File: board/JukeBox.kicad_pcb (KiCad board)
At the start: 2 copper layers, 90 x 90 mm, 81 parts, among them J1 USB_C_Receptacle_USB2.0, J2 Conn_01x03, J3 Conn_01x04, J4 Conn_01x08, J5 Conn_01x01, J6 Conn_01x03, J7 Conn_01x03, J8 Conn_01x01, SW1 SW_SPST, SW10 SW_SPST, SW11 SW_SPST, SW12 SW_SPST, SW2 SW_SPST, SW3 SW_SPST, SW4 SW_SPST, SW5 SW_SPST, SW6 SW_SPST, SW7 SW_SPST, SW8 SW_SPST, SW9 SW_SPST, U1 NCP1117-3.3_SOT223, U2 W25Q128JVS, U3 RP2040, Y1 ABLS-12.000MHZ-B4-T

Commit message: minor board adjustments
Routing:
- net VBUS: track 8.61 -> 13.8 mm
- net Net-(D29-Pad2): track 0.00 -> 1.95 mm
- net Net-(D30-Pad2): track 0.00 -> 1.95 mm
- net /QSPI_SCLK: track 31.4 -> 30.9 mm
- net /QSPI_SD3: track 33.4 -> 32.9 mm
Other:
- rule pad_to_mask_clearance: 0.051 -> 0

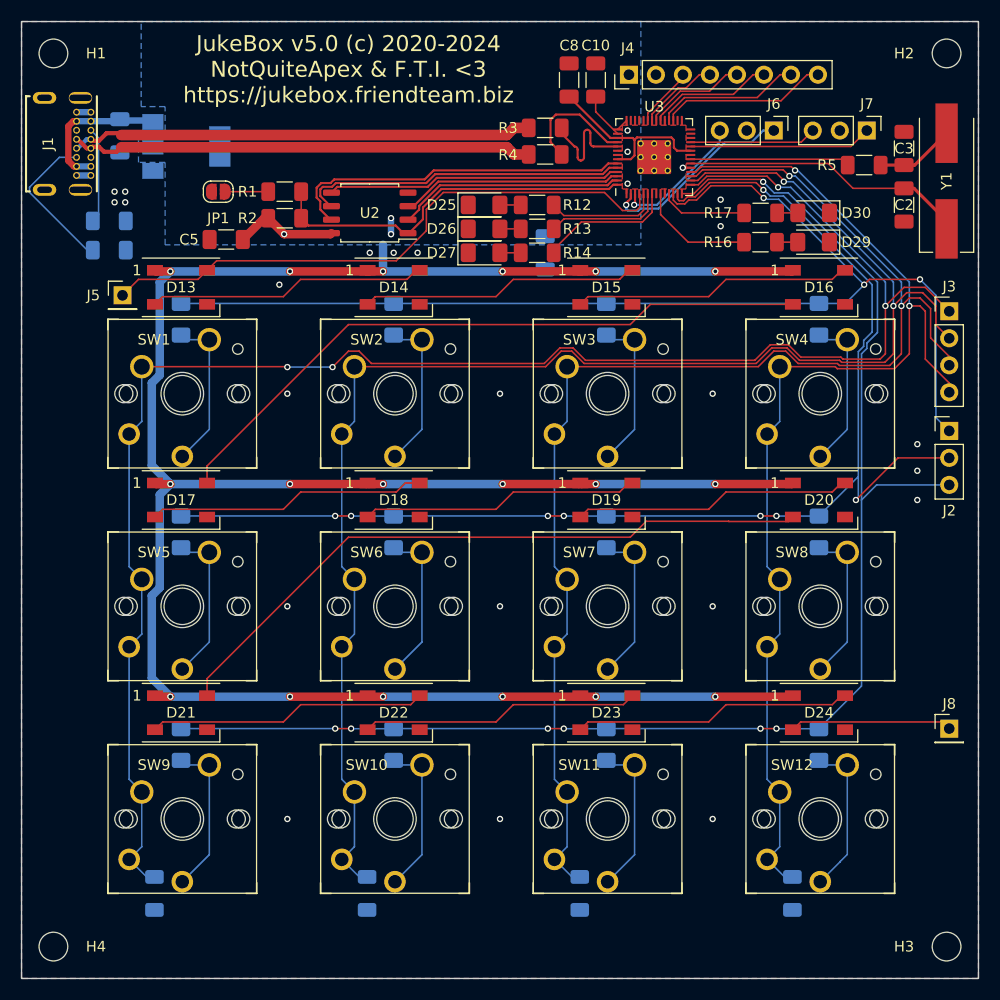
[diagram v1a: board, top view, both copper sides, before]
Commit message: move all pcb components to top layer
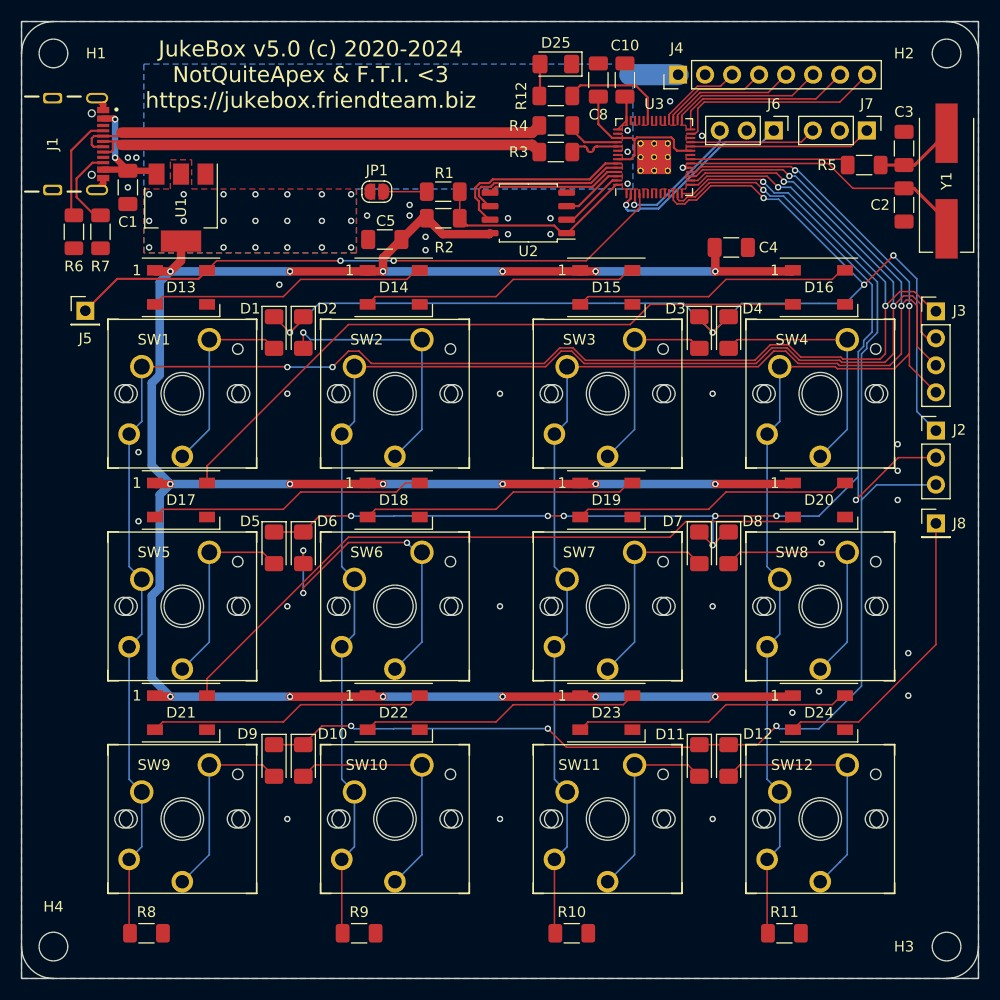
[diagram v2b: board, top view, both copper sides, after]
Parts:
- removed D26, D27, D29, D30: LED, Diode_SMD:D_1206_3216Metric_Pad1.42x1.75mm_HandSolder
- removed R13, R14, R16, R17: 200, Resistor_SMD:R_1206_3216Metric_Pad1.30x1.75mm_HandSolder
- C1, C4, D1, D10, D11, D12, D2, D3, D4, D5, D6, D7, D8, D9, R10, R11, R6, R7, R8, R9, U1: moved to F.Cu
- J1: value USB_C_Receptacle_USB2.0 -> USB4105-GF-A; footprint RP2040_minimal:GCT_USB4085-GF-A_REVA4 -> RP2040_minimal:GCT_USB4105-GF-A
- moved J8 19.3 mm to (253.6, 102.2)
- moved C4 17.5 mm to (234.3, 76.2), turned to 0 degrees
- moved C5 14.9 mm to (201.8, 75.5)
- moved JP1 14.9 mm to (201.0, 71.0)
- moved R1 14.9 mm to (207.3, 71.0)
- moved R2 14.9 mm to (207.3, 73.5)
- moved U2 14.9 mm to (215.3, 73.0)
- moved D25 14.9 mm to (217.8, 59.0), turned to 180 degrees
- moved R12 10.4 mm to (217.8, 62.0)
- moved D11 8.88 mm to (231.3, 124.5)
- moved D5 8.88 mm to (191.3, 104.5)
- moved D7 8.88 mm to (231.3, 104.5)
- moved D9 8.88 mm to (191.3, 124.5)
- moved D1 8.84 mm to (191.3, 84.2)
- moved D3 8.84 mm to (231.3, 84.2)
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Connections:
- J4 pad 3: /GPIO25 -> /GPIO21
- J4 pad 4: /GPIO24 -> /GPIO20
- J4 pad 5: /GPIO23 -> /GPIO19
- J4 pad 6: /GPIO22 -> /GPIO18
- J4 pad 7: /GPIO21 -> /GPIO17
- J4 pad 8: /GPIO20 -> /GPIO16
- R12 pad 1: /GPIO3 -> /GPIO25
- U3 pad 26: /RUN -> +3V3
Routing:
- net /GPIO16: track 0.00 -> 20.1 mm
- net /GPIO17: track 0.00 -> 17.2 mm
- net Net-(D6-Pad2): track 14.9 -> 31.1 mm, vias 0 -> 3
- net /QSPI_SS: track 35.4 -> 19.8 mm
- net /QSPI_SD1: track 21.4 -> 6.32 mm
- net /QSPI_SD0: track 27.7 -> 12.8 mm
- net /QSPI_SD3: track 32.9 -> 18.0 mm
- net /QSPI_SD2: track 20.9 -> 5.96 mm
- net /QSPI_SCLK: track 30.9 -> 16.0 mm
- net /GPIO18: track 0.00 -> 14.4 mm
- net /RGBDOUT: track 15.3 -> 28.2 mm
- net /GPIO5: track 12.8 -> 0.00 mm
- net /GPIO19: track 0.00 -> 12.3 mm
- net /GPIO22: track 11.8 -> 0.00 mm
- net /GPIO4: track 11.2 -> 0.00 mm
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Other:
- outline, holes or cut-outs redrawn

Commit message: add models to pcb, adjust some resistor placement
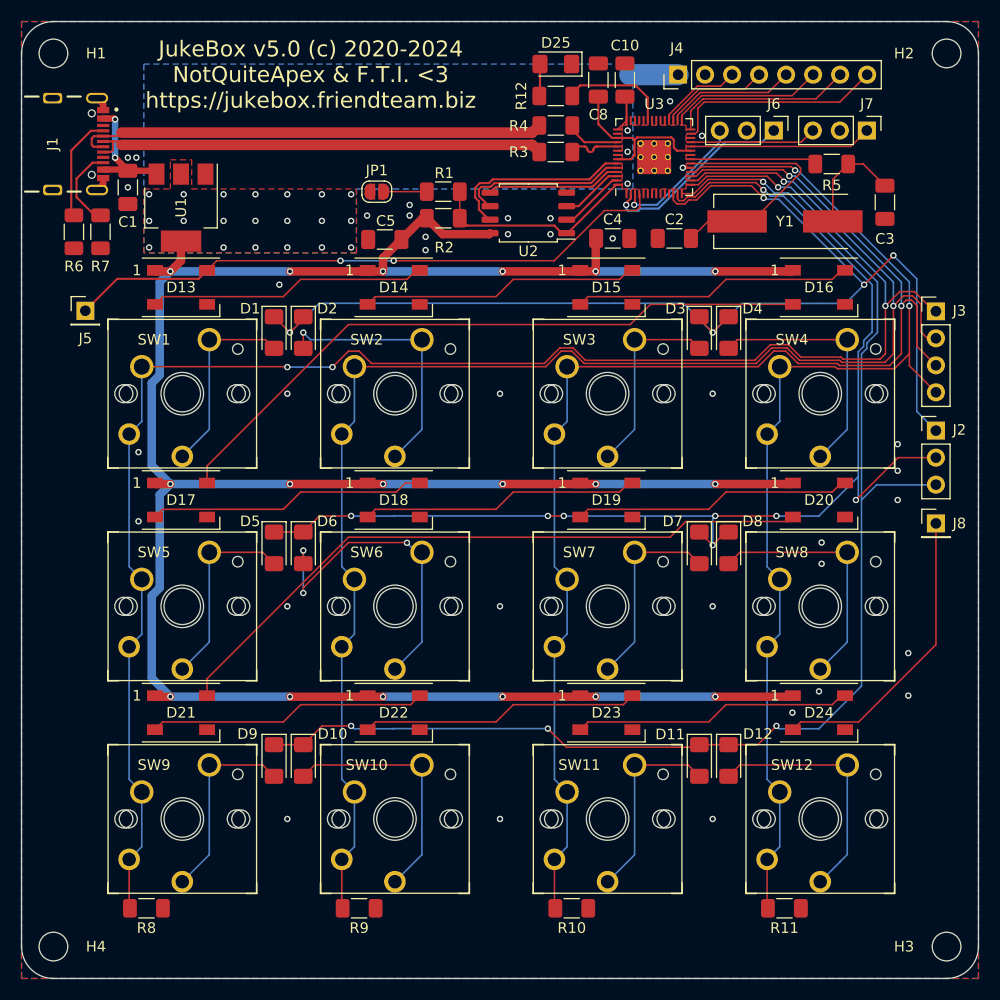
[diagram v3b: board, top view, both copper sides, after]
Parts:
- moved C2 21.8 mm to (229.0, 75.4), turned to 180 degrees
- moved Y1 15.7 mm to (239.4, 73.8), turned to 0 degrees
- moved C4 11.2 mm to (223.2, 75.4)
- moved C3 5.37 mm to (248.8, 72.0), turned to -90 degrees
- moved R5 3.05 mm to (243.8, 68.4)
- moved R10 2.35 mm to (219.3, 138.4)
- moved R11 2.35 mm to (239.3, 138.4)
- moved R8 2.35 mm to (179.3, 138.4)
- moved R9 2.35 mm to (199.3, 138.4)
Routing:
- net /XOUT: track 15.0 -> 11.9 mm
- net Net-(C3-Pad1): track 7.44 -> 10.3 mm
- net /XIN: track 27.0 -> 24.6 mm
- net /GPIO13: track 147.0 -> 144.7 mm
- net /GPIO14: track 128.3 -> 126.0 mm
- net /GPIO15: track 105.3 -> 103.0 mm
- net /GPIO12: track 164.9 -> 162.5 mm
- net +3V3: track 255.1 -> 256.0 mm
- net GND: vias 36 -> 37
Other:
- outline, holes or cut-outs redrawn

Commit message: minor adjustments
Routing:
- net /XIN: track 24.6 -> 23.8 mm
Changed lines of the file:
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@@
       (viasonmask false)
       (mode 1)
-      (useauxorigin false)
+      (useauxorigin true)
       (hpglpennumber 1)
       (hpglpenspeed 20)
@@
     (fp_line (start -1.6 -0.4) (end -1.6 0.8) (layer "F.Fab") (width 0.1))
     (fp_line (start 1.6 0.8) (end 1.6 -0.8) (layer "F.Fab") (width 0.1))
-    (pad "1" smd roundrect (at -1.4875 0 180) (size 1.425 1.75) (layers "F.Cu" "F.Paste" "F.Mask") (roundrect_rratio 0.175439)
+    (pad "1" smd roundrect (at -1.4875 0 180) (size 1.425 1.75) (layers "F.Cu" "F.Paste" "F.Mask") (roundrect_rratio 0.1754392982)
       (net 1 "GND") (pinfunction "K") (pintype "passive"))
-    (pad "2" smd roundrect (at 1.4875 0 180) (size 1.425 1.75) (layers "F.Cu" "F.Paste" "F.Mask") (roundrect_rratio 0.175439)
+    (pad "2" smd roundrect (at 1.4875 0 180) (size 1.425 1.75) (layers "F.Cu" "F.Paste" "F.Mask") (roundrect_rratio 0.1754392982)
       (net 69 "Net-(D25-Pad2)") (pinfunction "A") (pintype "passive"))
     (model "${KICAD6_3DMODEL_DIR}/Diode_SMD.3dshapes/D_1206_3216Metric.wrl"
@@
     (fp_line (start 1.6 -0.8) (end 1.6 0.8) (layer "F.Fab") (width 0.1))
     (fp_line (start -1.6 -0.8) (end 1.6 -0.8) (layer "F.Fab") (width 0.1))
-    (pad "1" smd roundrect (at -1.55 0 180) (size 1.3 1.75) (layers "F.Cu" "F.Paste" "F.Mask") (roundrect_rratio 0.192308)
+    (pad "1" smd roundrect (at -1.55 0 180) (size 1.3 1.75) (layers "F.Cu" "F.Paste" "F.Mask") (roundrect_rratio 0.1923076923)
       (net 73 "/GPIO25") (pintype "passive"))
-    (pad "2" smd roundrect (at 1.55 0 180) (size 1.3 1.75) (layers "F.Cu" "F.Paste" "F.Mask") (roundrect_rratio 0.192308)
+    (pad "2" smd roundrect (at 1.55 0 180) (size 1.3 1.75) (layers "F.Cu" "F.Paste" "F.Mask") (roundrect_rratio 0.1923076923)
       (net 69 "Net-(D25-Pad2)") (pintype "passive"))
     (model "${KICAD6_3DMODEL_DIR}/Resistor_SMD.3dshapes/R_1206_3216Metric.wrl"
@@
   (via (at 176.39 67.8) (size 0.6) (drill 0.35) (layers "F.Cu" "B.Cu") (net 2))
   (segment (start 176.39 64.2) (end 176.39 67.8) (width 0.6) (layer "B.Cu") (net 2))
-  (segment (start 235.682463 74.4) (end 234.89 74.4) (width 0.15) (layer "F.Cu") (net 3))
   (segment (start 230.5275 68.35) (end 240.432463 68.35) (width 0.15) (layer "F.Cu") (net 3))
   (segment (start 232.1525 73.8) (end 230.5525 75.4) (width 0.15) (layer "F.Cu") (net 3))
@@
     (polygon
       (pts
-        (xy 183.59 70.75)
+        (xy 183.39 70.75)
         (xy 199.09 70.75)
         (xy 199.09 76.75)
         (xy 179.09 76.75)
         (xy 179.09 70.75)
-        (xy 181.59 70.75)
-        (xy 181.59 69.75)
-        (xy 181.59 68.75)
-        (xy 181.59 68)
-        (xy 183.59 68)
+        (xy 181.79 70.75)
+        (xy 181.79 69.75)
+        (xy 181.79 68.75)
+        (xy 181.79 68.4)
+        (xy 183.39 68.4)
       )
     )

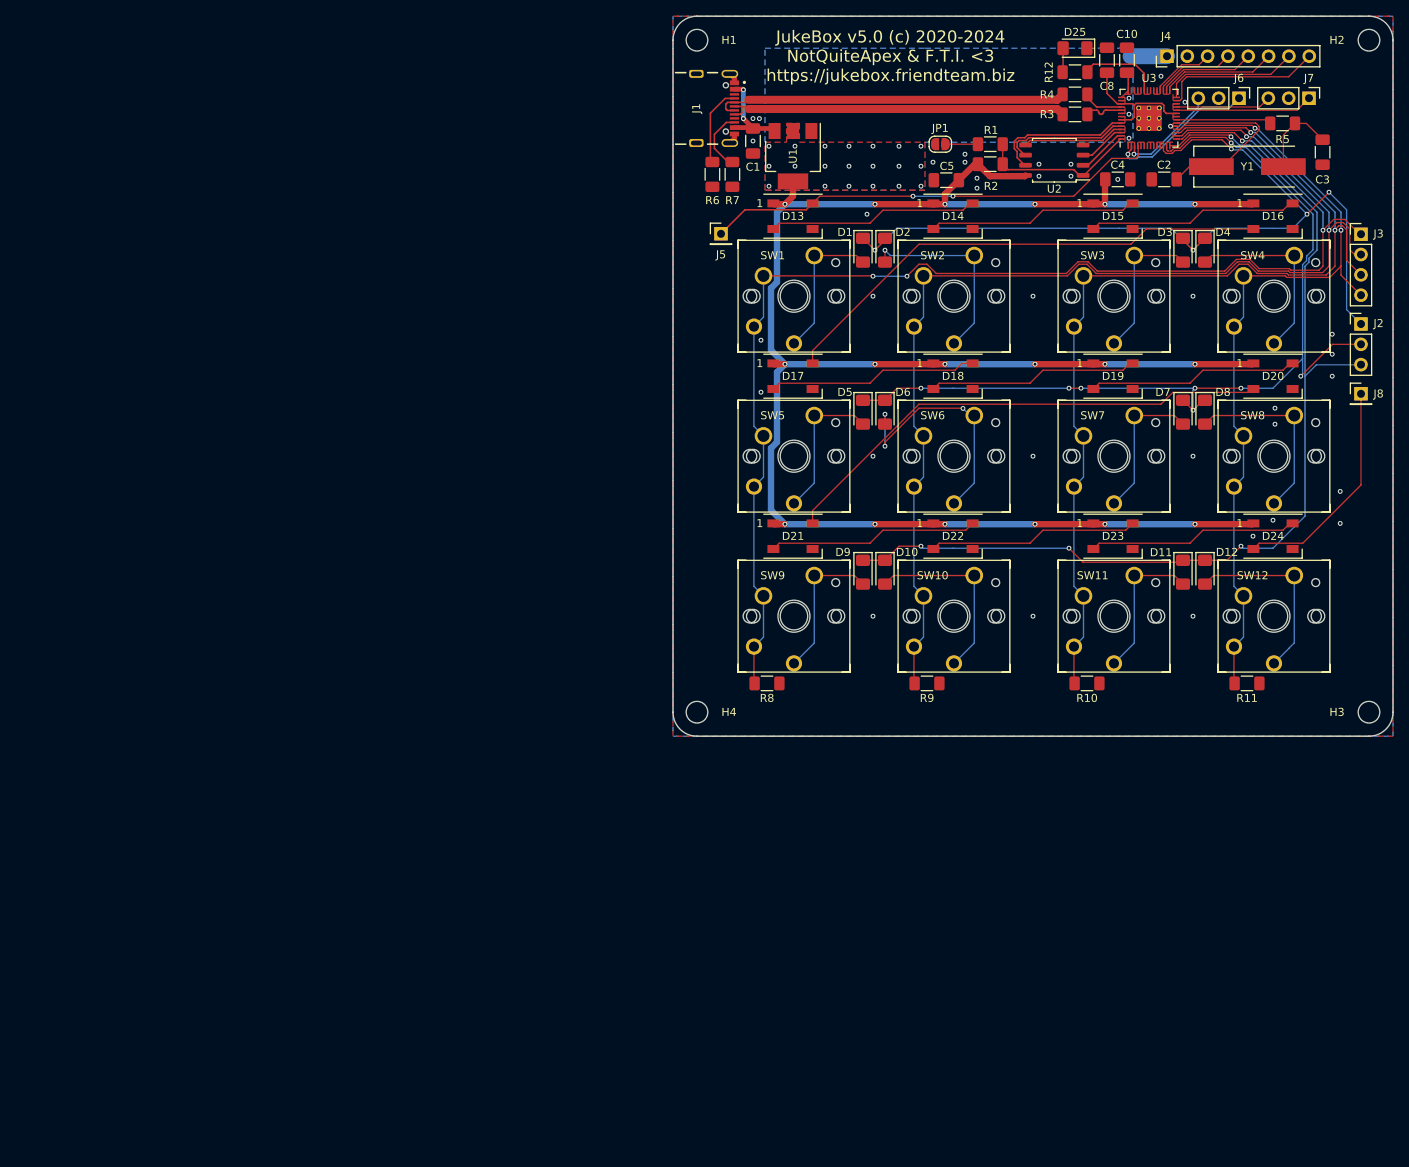
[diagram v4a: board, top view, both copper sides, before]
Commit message: fix pcb for new footprints, remove old files, update readme
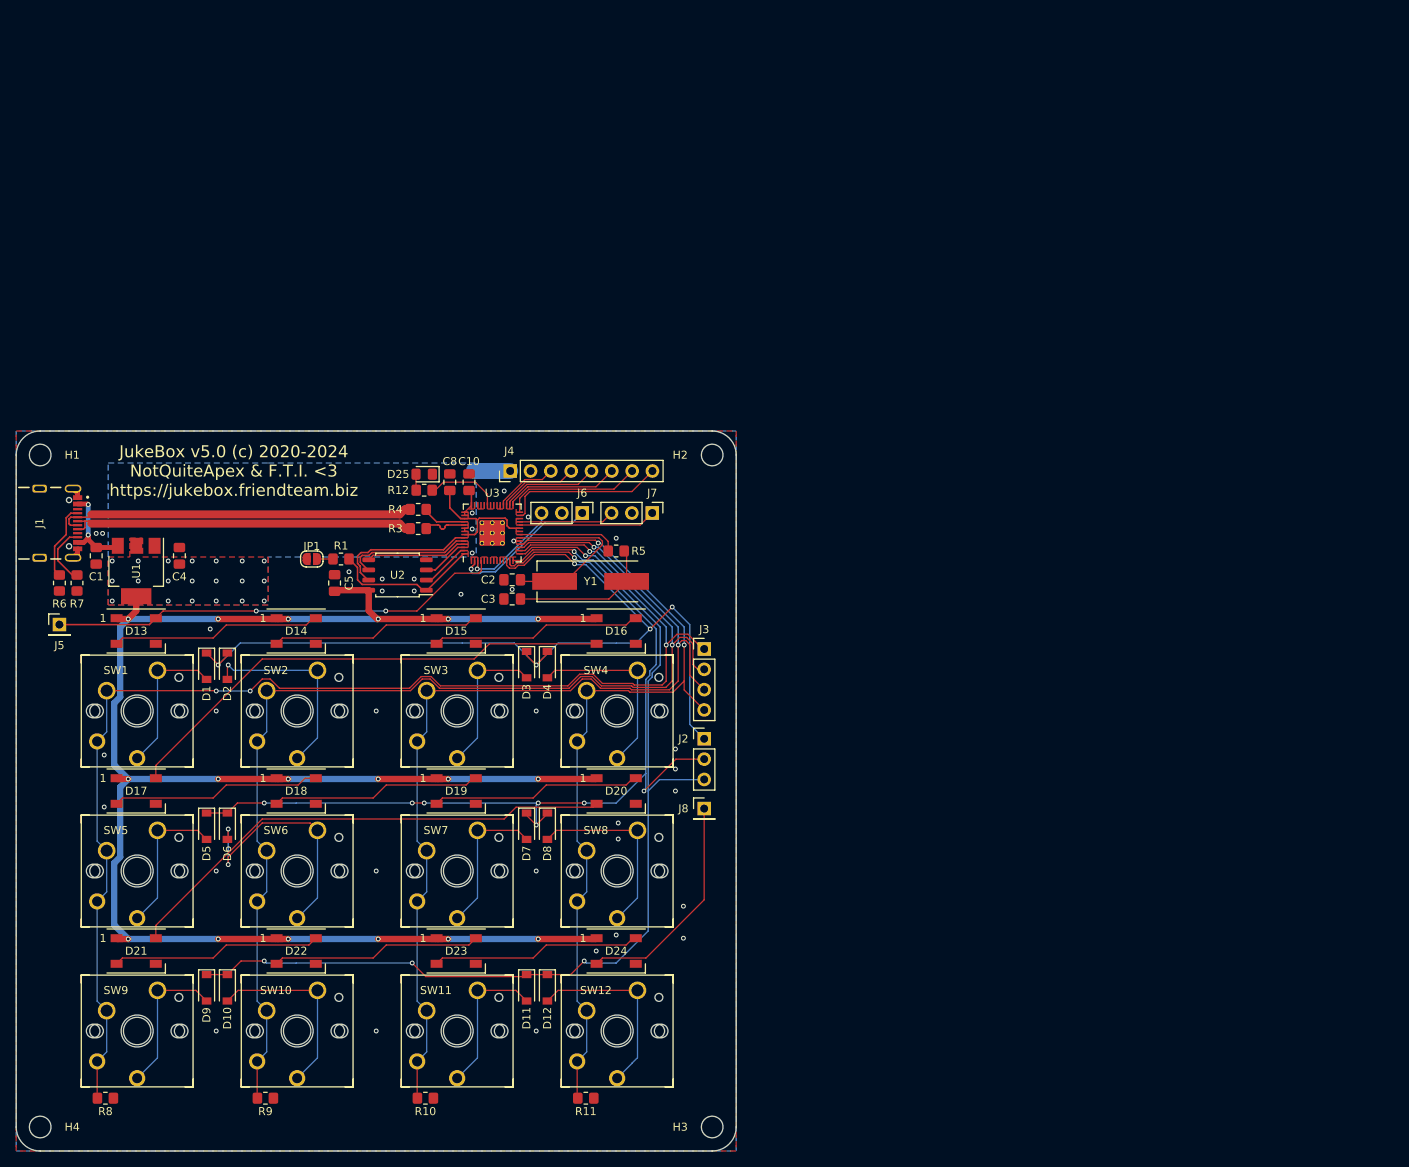
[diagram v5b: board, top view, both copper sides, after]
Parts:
- removed R2: DNF, Resistor_SMD:R_1206_3216Metric_Pad1.30x1.75mm_HandSolder
- C1, C10, C2, C3, C4, C5, C8: footprint Capacitor_SMD:C_1206_3216Metric_Pad1.33x1.80mm_HandSolder -> Capacitor_SMD:C_0805_2012Metric_Pad1.18x1.45mm_HandSolder
- D1, D10, D11, D12, D2, D3, D4, D5, D6, D7, D8, D9: footprint Diode_SMD:D_1206_3216Metric_Pad1.42x1.75mm_HandSolder -> Diode_SMD:D_SOD-123
- D25: footprint Diode_SMD:D_1206_3216Metric_Pad1.42x1.75mm_HandSolder -> Diode_SMD:D_0805_2012Metric_Pad1.15x1.40mm_HandSolder
- R1, R10, R11, R12, R3, R4, R5, R6, R7, R8, R9: footprint Resistor_SMD:R_1206_3216Metric_Pad1.30x1.75mm_HandSolder -> Resistor_SMD:R_0805_2012Metric_Pad1.20x1.40mm_HandSolder
- moved C4 126.4 mm to (105.9, 122.5), turned to 90 degrees
- moved C3 115.7 mm to (147.5, 127.8), turned to 180 degrees
- moved R5 99.0 mm to (160.5, 121.8)
- moved C10 97.7 mm to (142.1, 113.2)
- moved C8 97.6 mm to (139.7, 113.2)
- moved R10 97.6 mm to (136.6, 190.2)
- moved R8 97.6 mm to (96.6, 190.2)
- moved R9 97.6 mm to (116.6, 190.2)
- moved R11 97.6 mm to (156.7, 190.2)
- moved D2 97.3 mm to (111.9, 136.2)
- moved D10 97.2 mm to (111.9, 176.4)
- moved D12 97.2 mm to (151.9, 176.4)
- moved D25 97.2 mm to (136.5, 112.2)
- moved D4 97.2 mm to (151.9, 136.1)
- moved D1 97.1 mm to (109.3, 136.2)
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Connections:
- JP1 pad 1: /~{USB_BOOT} -> GND
- JP1 pad 2: GND -> /~{USB_BOOT}
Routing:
- net Net-(C3-Pad1): track 10.3 -> 18.1 mm
- net +3V3: track 256.0 -> 248.3 mm
- net /~{USB_BOOT}: track 4.05 -> 2.00 mm
- net /QSPI_SS: track 19.8 -> 18.9 mm
- net Net-(D6-Pad2): track 31.1 -> 32.0 mm, vias 3 -> 2
- net Net-(D25-Pad2): track 2.78 -> 2.01 mm
- net /XOUT: track 11.9 -> 12.6 mm
- net /GPIO25: track 10.0 -> 9.35 mm
- net /XIN: track 23.8 -> 23.2 mm
- net /GPIO2: track 57.5 -> 56.8 mm
- net /USB_D-: track 44.4 -> 44.9 mm
- net /USB_D+: track 43.2 -> 43.8 mm
- net /USB_R_D+: track 5.03 -> 5.54 mm
- net GND: vias 37 -> 34
